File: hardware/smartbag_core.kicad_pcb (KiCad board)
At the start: 4 copper layers, 196 x 20 mm, 113 parts, among them J1 FFC optics, 12 way, J2 Jauch LP523450JU 950mAh, J3 Qi RX coil, J4 FFC FSR matrix, 24 way, J5 SWD debug, Q1 SI2302CDS-T1-GE3, U1 nRF54L15-QFAA-R, U11 BQ51013BRHLR, U2 Acconeer A121, U3 nPM1300-QEAA-R7, U4 BMI270, U5 DRV5032FBDBZR, U6 Acconeer A121, U7 CD74HC4067SM96, U8 TLV9064IPWR, U9 TLV9064IPWR, Y1 32 MHz Cl=8pF, Y2 24 MHz, Y3 24 MHz, Y4 32.768 kHz Cl=9pF

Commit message: Two of the three closed: the escapes were the missing half
U1.10 reaches its decoupling capacitor through two B.Cu segments from the
escape via the tidy-up had removed. FSR_R2 needed one drop at (242.631,
147.295) — a B.Cu track that had finished exactly on an F.Cu pad.

3 unconnected -> 1, still 0 clearance violations and 0 shorts.

⛔ And two more of the same mistake on the way, both mine: a B.Cu track ending
on an F.Cu pad connects nothing, and I laid one before checking. The
destination's layer is part of the destination.

Co-Authored-By: Claude Opus 5 <noreply@anthropic.com>
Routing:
- net VDD_3V3: track 309.5 -> 312.0 mm
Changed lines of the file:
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@@
+	)
+	(segment
+		(start 189.61 149.39)
+		(end 188.6108 148.3914)
+		(width 0.1)
+		(layer "B.Cu")
+		(net "VDD_3V3")
 	)
 	(segment
@@
 		(layer "B.Cu")
 		(net "VDD_3V3")
+	)
+	(segment
+		(start 190.7 149.4)
+		(end 189.61 149.39)
+		(width 0.1)
+		(layer "B.Cu")
+		(net "VDD_3V3")

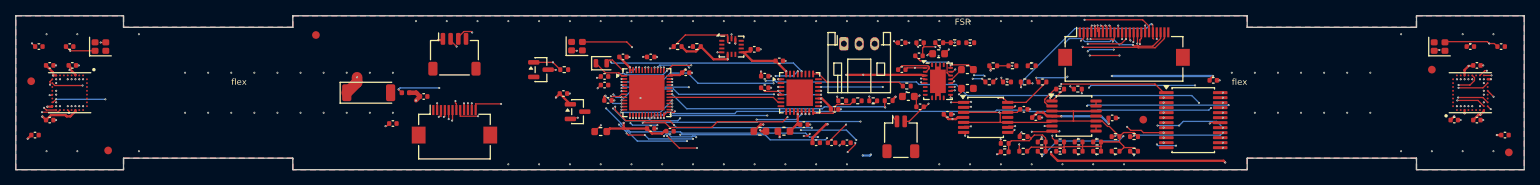
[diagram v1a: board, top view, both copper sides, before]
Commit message: Zero. Six layers, and the number that justified them
  U1 pin 22, free cells reachable, by breadth-first search on a 0.1 mm grid:

    four layers   F.Cu 23    In2 41   B.Cu 2                =  66
    six layers    F.Cu 372   In2 3    In3 52    B.Cu 345    = 772

Four copper layers meant three routable ones — In1 is the RF reference and
nothing is routed there, enforced by marking it a `power` layer in the Specctra
export after the first routed board put 34% of its tracks on it. A QFN48 with
thirty-five escapes exhausts three layers, and pin 22 finished walled into
0.4 mm2 with no copper of its own net anywhere in it. Straight links, L-bends,
two-segment paths with the corner searched on a grid, moving the escape via
anywhere within 2.4 mm of the pad, and the maze router itself: none of them was
the problem. Neither was the routing. The board was full.

  F.Cu / In1(GND) / In2 / In3 / In4(GND) / B.Cu

The signal pair sits between the two planes, so no signal layer is ever more
than one dielectric from a reference — which is why In3 and In4 were added
together rather than making In3 a third signal layer against nothing. Both
planes are marked `power` in the DSN, so the router may via through them and may
not route on them.

  0 unconnected pads. 0 clearance violations. 0 shorts. ERC clean.

What is left in the report is 2 library-mismatch warnings that have been
overridden since the A121 footprint was transcribed, 3 silkscreen clips, and 6
dangling vias — five of which are escapes that drop_dangling now deliberately
spares, because removing two of them is what stranded these pins in the first
place.

⚠️ On a rigid-flex six layers is not the usual four-to-six conversation. It costs
more than on FR4 and whether the flex tails carry all six is a question for the
quote; the rigid islands need six. fab/README-FAB.md says so, with the table.

Co-Authored-By: Claude Opus 5 <noreply@anthropic.com>
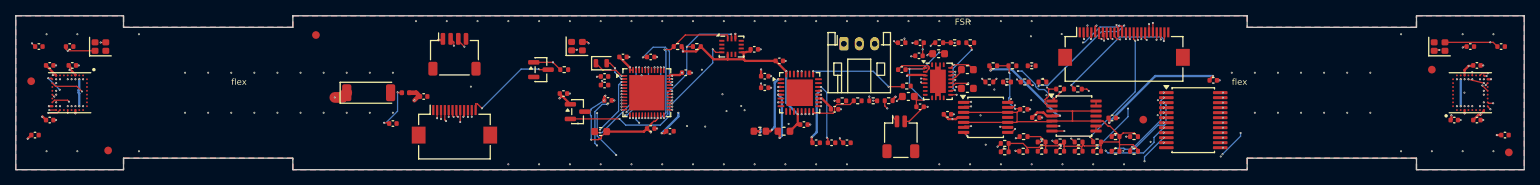
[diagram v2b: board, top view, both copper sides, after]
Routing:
- net VSYS: track 87.3 -> 63.1 mm, vias 6 -> 7
- net SPI_MOSI: track 216.0 -> 196.6 mm, vias 10 -> 6
- net I2C_SDA: track 82.0 -> 66.6 mm, vias 6 -> 4
- net VDD_3V3: track 312.0 -> 297.8 mm, vias 24 -> 29
- net VDD_CAM: track 76.1 -> 62.8 mm
- net VBUSOUT: track 19.2 -> 7.96 mm, vias 3 -> 2
- net FSR_C1: track 34.5 -> 45.7 mm, vias 3 -> 4
- net ADC2: track 73.7 -> 63.9 mm, vias 5 -> 3
- net FSR_R1: track 41.4 -> 32.4 mm, vias 5 -> 3
- net TOF_XSHUT: track 39.2 -> 31.4 mm, vias 2 -> 3
- net VQI: track 29.0 -> 22.2 mm, vias 4 -> 3
- net FSR_C7: track 27.5 -> 20.7 mm
- net VDD_1V8: track 242.2 -> 235.5 mm, vias 20 -> 18
- net FSR_C3: track 35.6 -> 29.1 mm
- net SPI_SCK: track 212.8 -> 206.3 mm, vias 6 -> 8
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- added copper zone on In4.Cu, net GND
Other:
- copper layers 4 -> 6

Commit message: The finishing is part of the pipeline now, because it was not
Regenerating the board from its session file threw away everything that had
taken it to zero: a .ses holds what the ROUTER did, and five of the connections
on this board were closed after it. The rebuild came back with five open and
still looked routed.

route.sh and reroute_from_session.sh now run the four finishing steps in the
order that matters — --tidy first because it decides which escape vias survive,
--link before the maze router because the maze router answers a question those
gaps are not asking, repairs.py last because it lays copper no search finds.

repairs.py gained polyline repairs and carries the two paths that close U1
pins 10 and 22: found by breadth-first search on a 0.1 mm grid, checked by DRC,
written down so the next regeneration keeps them.

Silkscreen moved off J2's through-hole pads — the text had been tracking a
connector by hand and the connector moved twice — and now says 6L rigid-flex,
which it is.

  0 unconnected. 0 clearance violations. 0 shorts. 6 warnings, all known:
  2 A121 library mismatches overridden since the footprint was transcribed,
  and 4 escape vias drop_dangling spares on purpose.

Co-Authored-By: Claude Opus 5 <noreply@anthropic.com>
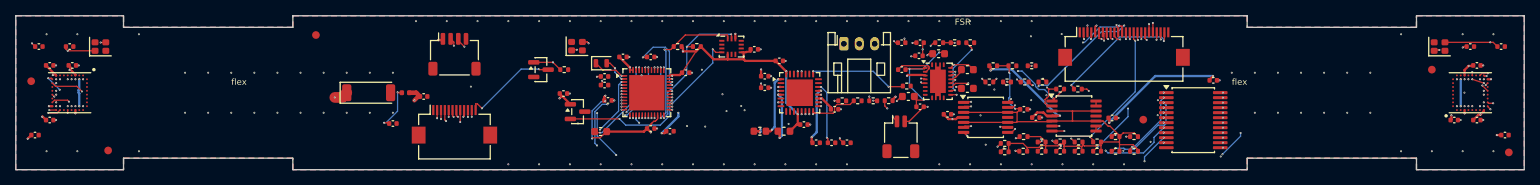
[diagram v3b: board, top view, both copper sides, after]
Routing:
- net VDD_3V3: track 297.8 -> 299.2 mm, vias 29 -> 27
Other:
- board text added: "tagless inventory - 6L rigid-flex"
- board text removed: "tagless inventory - 4L rigid-flex"

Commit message: Six copper layers in the zip, and the layer list no longer typed by hand
The fabrication package was plotting a six-layer board as four. tools/fab.sh
named the copper layers in a string, the string was right for four, the stackup
became six, and In3 and In4 were simply not in the gerbers. The comment directly
above that string warned about exactly this failure — "the default set is for a
2-layer board and would silently drop the inner planes" — and then did not save
it, because a warning about a hand-typed list is still a hand-typed list.

It reads the layer table out of the .kicad_pcb now. A board file cannot be wrong
about how many copper layers it has.

  copper: F.Cu,In1.Cu,In2.Cu,In3.Cu,In4.Cu,B.Cu
  fab/  2.1M, drc-report.txt inside it says 0 unconnected

Everything else in fab/ regenerated against the finished board: gerbers, both
drill files, placement, the BOM, the DRC and ERC reports, and a fab note that
now carries the stackup table and the measurement that justified it.

Co-Authored-By: Claude Opus 5 <noreply@anthropic.com>
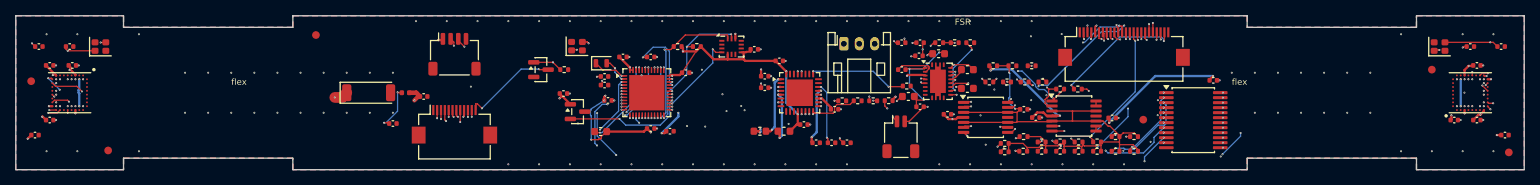
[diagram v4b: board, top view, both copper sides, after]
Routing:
- net VDD_3V3: track 299.2 -> 293.8 mm, vias 27 -> 28
- net GND: track 1.58 -> 0.71 mm

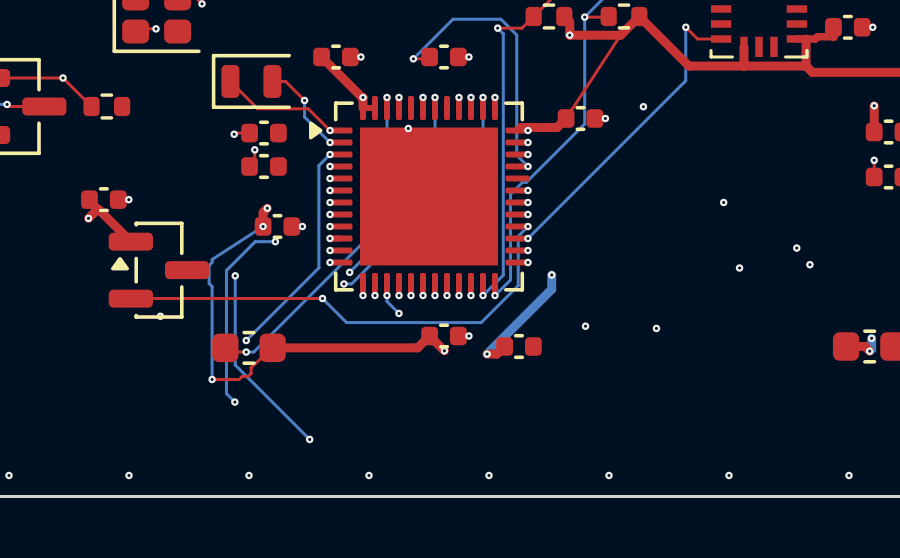
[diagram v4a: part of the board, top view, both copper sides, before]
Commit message: Every frame rebuilt, and the check that would have hidden it
The films are re-rendered from scratch — 696 frames across five shots plus two
vertical ones, not re-encoded from yesterday's — so smartbag.mp4,
smartbag_sequence.mp4 and the 9:16 discovery clip all show the six-layer board
and a bag with no handle arcing across its own mouth.

exploded.png was rendered two seconds before scenes.py was edited and section.png
ten seconds after. The staleness check, which now reads a film's oldest FRAME
rather than the mp4's timestamp, caught the two-second one.

  all constraints hold

Co-Authored-By: Claude Opus 5 <noreply@anthropic.com>
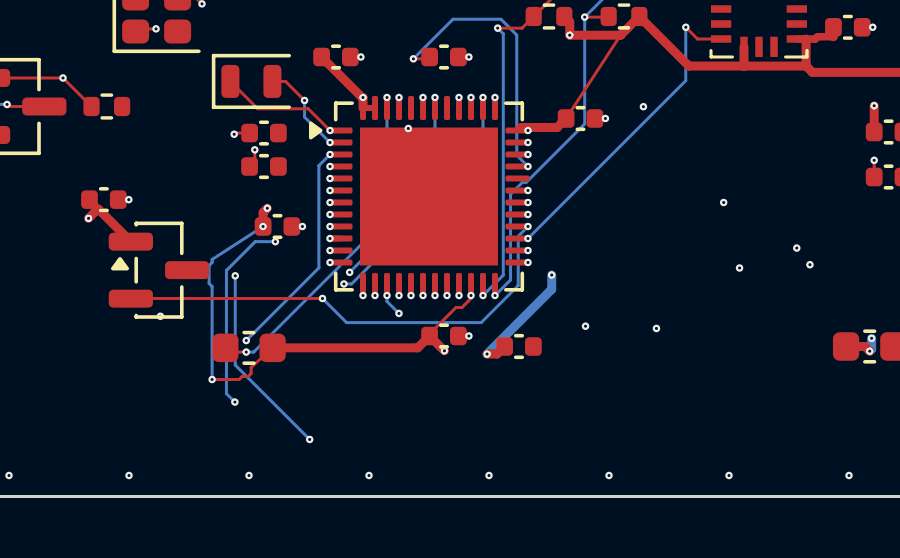
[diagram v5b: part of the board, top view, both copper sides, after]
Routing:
- net VDD_3V3: track 293.8 -> 298.4 mm
